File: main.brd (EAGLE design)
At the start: 34.3 x 32.7 mm, 14 parts, among them IC1 TS520550, IC2 TINY13-20SSU, J1 AVR_SPI_PROG_5X2PTH, T1 BST82-1

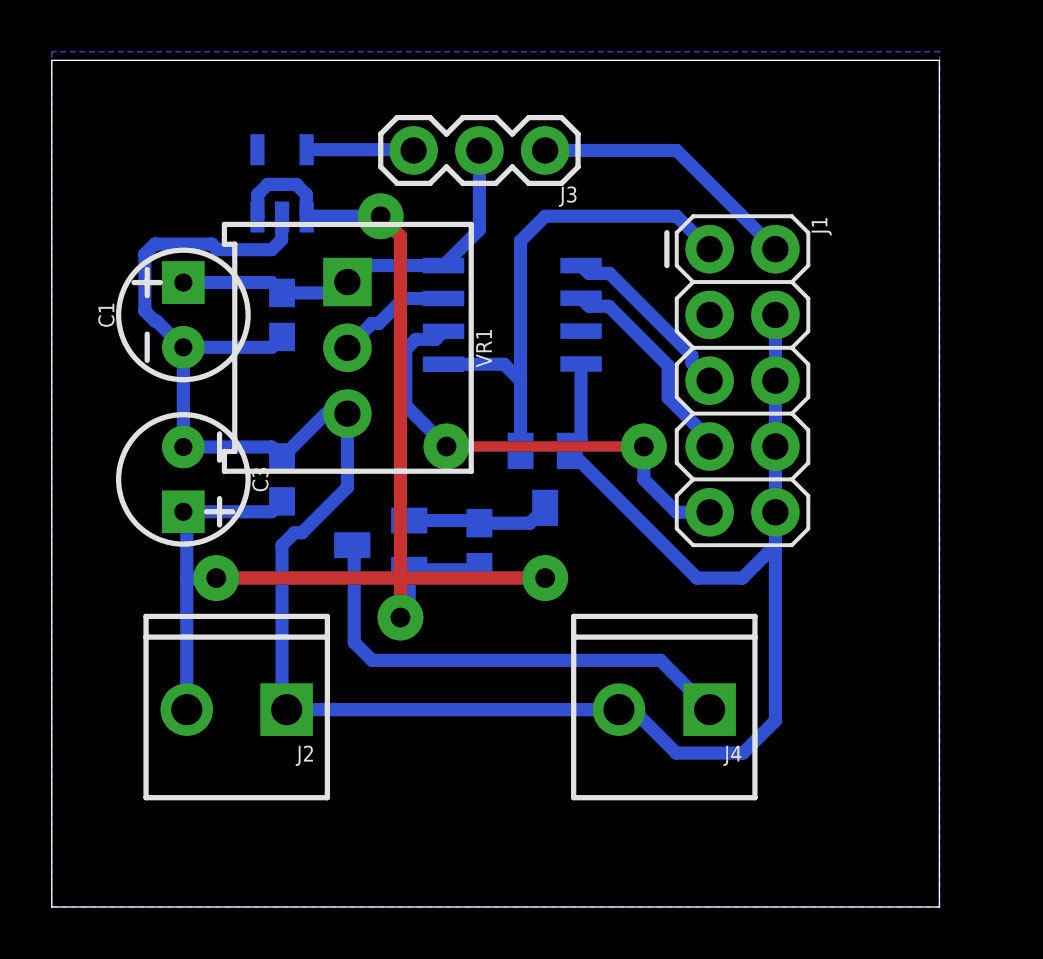
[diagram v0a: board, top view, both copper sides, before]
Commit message: Larger MOSFET, smaller SPI header and a rearrange.
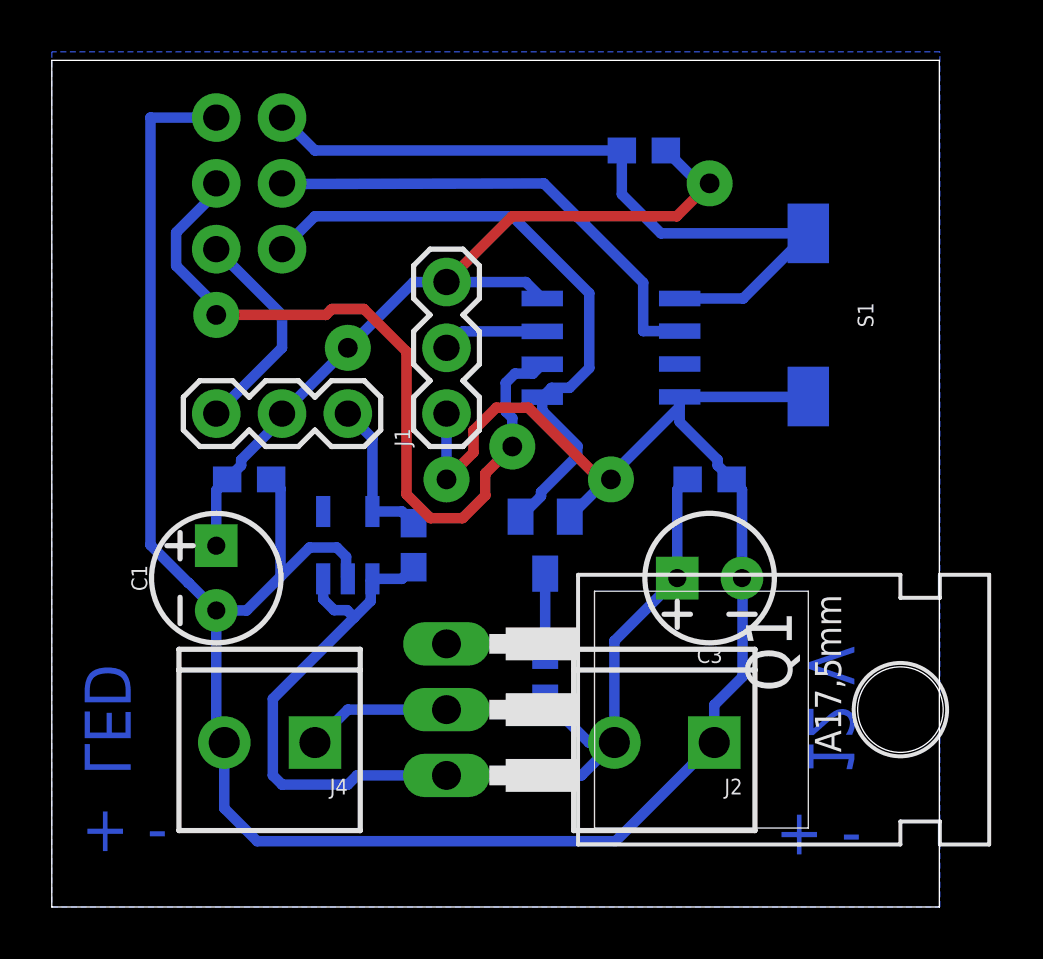
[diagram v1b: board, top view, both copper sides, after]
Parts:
- removed U$1: A1SHB, Test:SOT23
- removed VR1: 10k, SparkFun-Resistors:TRIMPOT-PTH-3386U
- added C5: 0.1uF, SparkFun-Capacitors:0603
- added J5: AVR_SPI_PROG_3X2NS, SparkFun-Connectors:2X3-NS
- added Q1: IRF4905, transistor-power:TO220BH
- added R2: 1k, SparkFun-Resistors:0603
- added S1: MOMENTARY-SWITCH-SPST-SMD-6.0X3.5MM, SparkFun-Switches:TACTILE_SWITCH_SMD_6.0X3.5MM
- J1: value AVR_SPI_PROG_5X2PTH -> (none); device SparkFun-Connectors:2X5 -> SparkFun-Connectors:1X03
- moved C3 20.7 mm to (25.4, 12.7), turned to 180 degrees
- moved J2 16.6 mm to (25.4, 6.35)
- moved C4 16.5 mm to (25.4, 16.5), turned to 180 degrees
- moved J3 16.3 mm to (6.35, 19.1), turned to 0 degrees
- moved J4 15.3 mm to (10.2, 6.35)
- moved IC1 14.2 mm to (11.4, 14.0)
- moved J1 12.0 mm to (15.2, 19.1), turned to 90 degrees
- moved C1 10.2 mm to (6.35, 12.7)
- moved C2 6.48 mm to (7.62, 16.5), turned to 180 degrees
- moved R1 5.68 mm to (19.1, 8.89)
- moved IC2 4.02 mm to (21.6, 21.6)
- moved T1 2.54 mm to (19.1, 14.0)
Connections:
- net +5V: now also J1.3, R2.2; no longer VR1.1
- net 5VREG: now also C5.1
- net 5VSPI: now also J5.2; no longer J1.2
- net CLK: now also J5.3; no longer J1.7
- net GND: now also J1.1, J5.6, S1.1; no longer J1.10, J1.4, J1.6, J1.8, VR1.3
- net MISO: now also J5.4; no longer J1.9
- net MOSI: now also J5.1; no longer J1.1
- net N$1: now also Q1.D; no longer U$1.3
- net N$2: now also J1.2; no longer VR1.2
- net N$3: now also Q1.G; no longer U$1.1
- net RESET: now also J5.5, R2.1, S1.2; no longer J1.5
- net VCC: now also C5.2, Q1.S; no longer U$1.2
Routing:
- net RESET: track 6.97 -> 29.2 mm
- net +5V: track 15.7 -> 32.5 mm, vias 0 -> 2
- net VCC: track 55.7 -> 41.9 mm, vias 4 -> 0
- net N$1: track 18.6 -> 5.61 mm
- net MISO: track 18.1 -> 30.4 mm
- net GND: track 88.5 -> 100.1 mm, vias 0 -> 2
- net CLK: track 8.41 -> 18.8 mm
- net MOSI: track 19.6 -> 25.4 mm
- net 5VSPI: track 10.5 -> 8.45 mm
- net 5VREG: track 4.18 -> 5.95 mm
- net N$3: track 5.54 -> 7.11 mm
- net N$2: track 4.50 -> 3.96 mm
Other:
- board text added: "- +"
- board text added: "12 V"
- board text added: "LED"
